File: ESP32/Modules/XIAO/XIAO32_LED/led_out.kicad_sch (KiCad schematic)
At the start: 3 parts, among them U3 74AHCT125

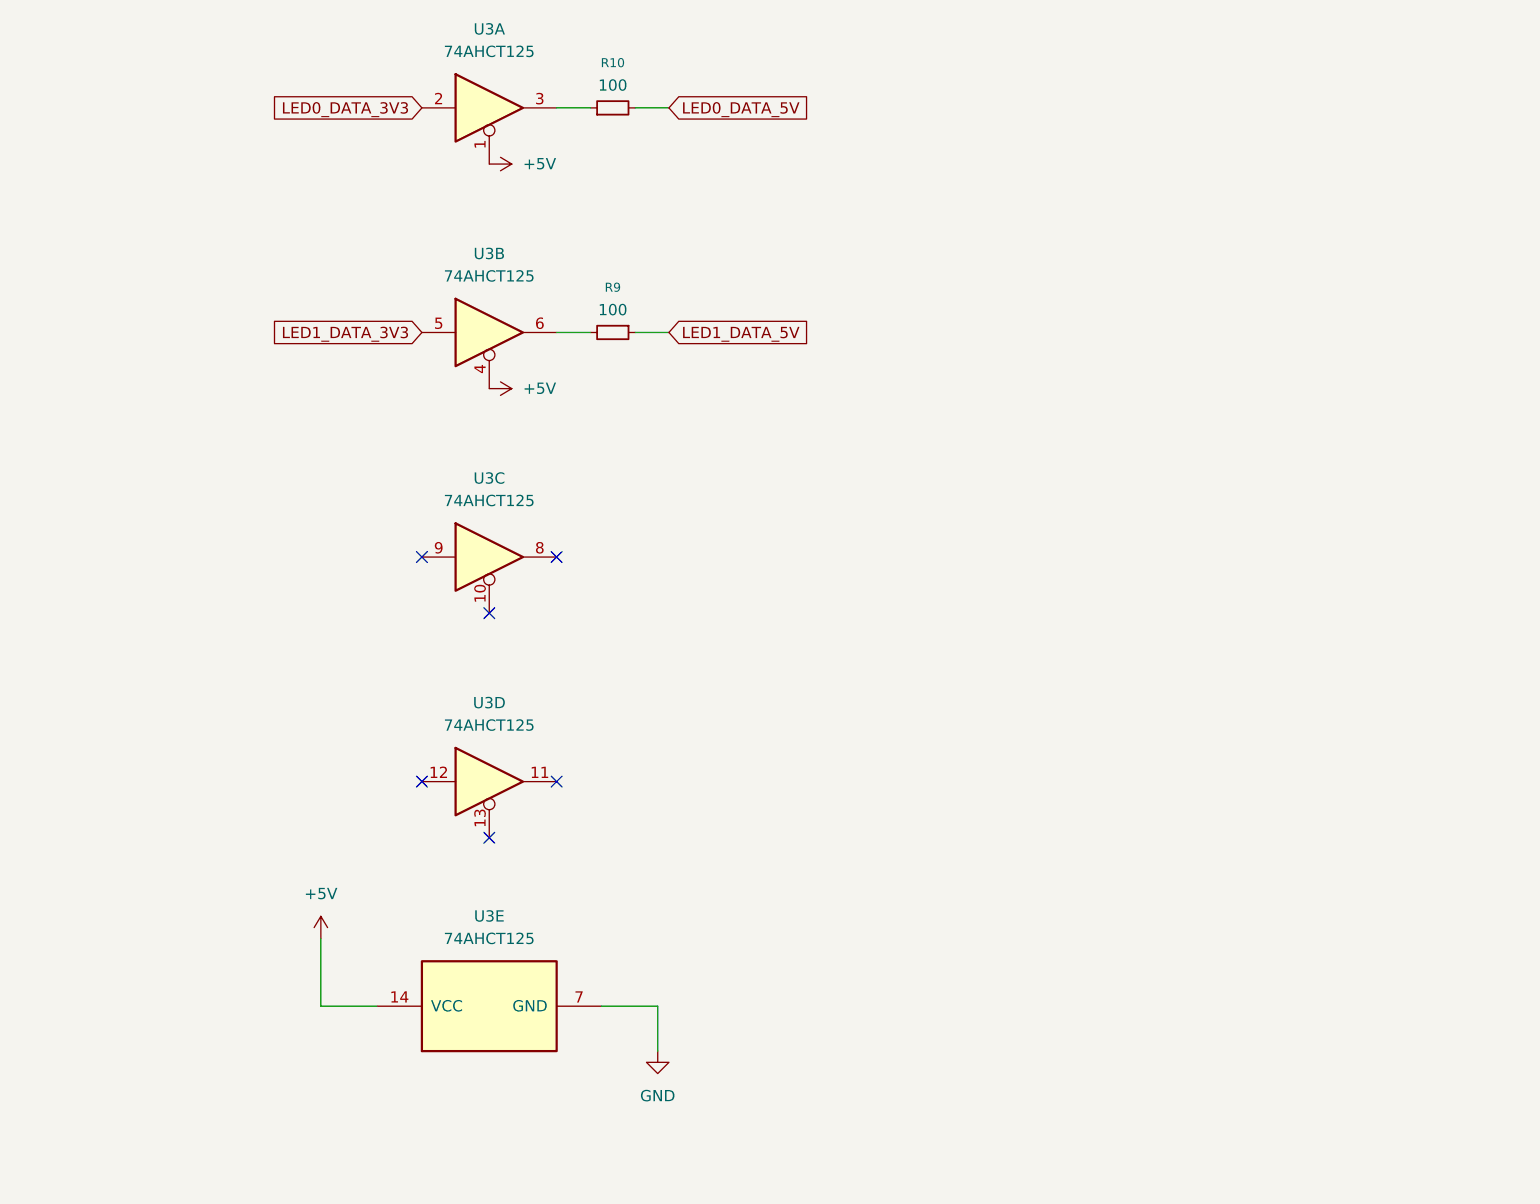
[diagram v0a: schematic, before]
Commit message: XIAO32_LED: Convert sch to hierarchical pins
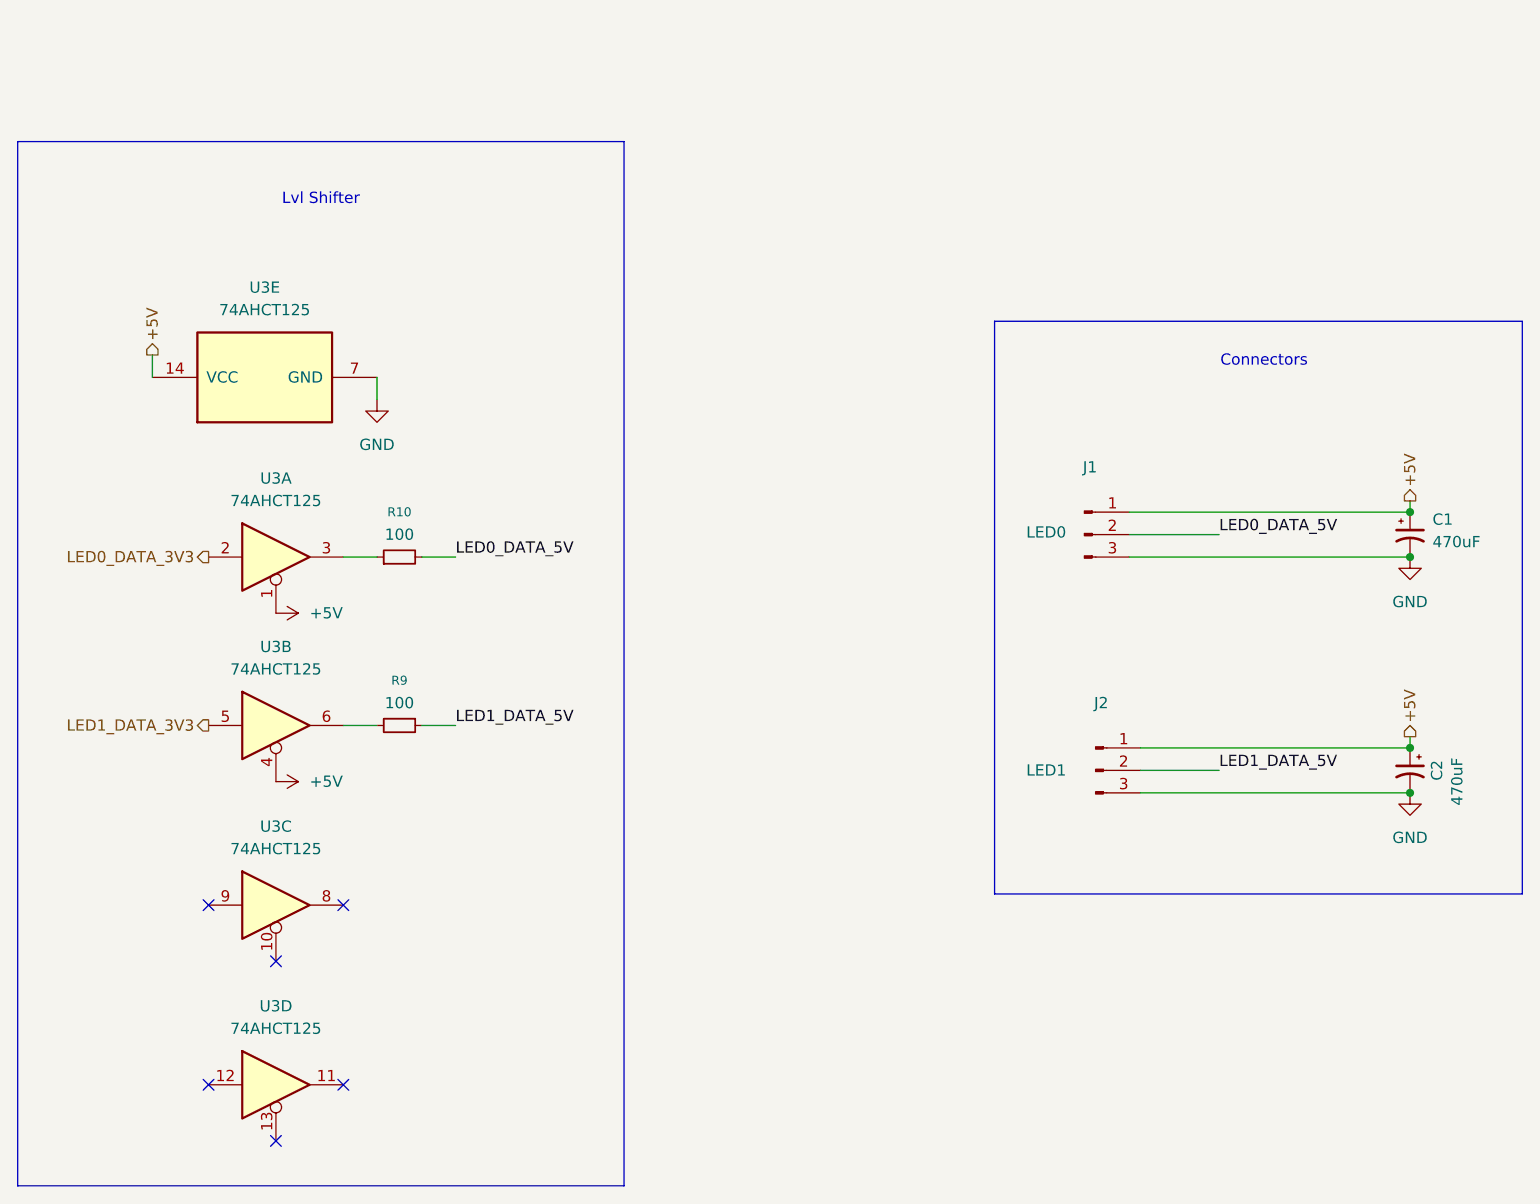
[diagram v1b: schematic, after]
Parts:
- added C1, C2: 470uF, symbol Device:C_Polarized_Small_US
- added J1: LED0, symbol Connector:Conn_01x03_Pin
- added J2: LED1, symbol Connector:Conn_01x03_Pin
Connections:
- net +5V: now also C1.1, C2.1, J1.1 (Pin_1), J2.1 (Pin_1)
- net GND: now also C1.2, C2.2, J1.3 (Pin_3), J2.3 (Pin_3)
- net LED0_DATA_5V: now also J1.2 (Pin_2)
- net LED1_DATA_5V: now also J2.2 (Pin_2)
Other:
- note added: "Connectors"
- note added: "Lvl Shifter"
- moved on the sheet: R10, R9, U3A, U3B, U3C, U3D, U3E
